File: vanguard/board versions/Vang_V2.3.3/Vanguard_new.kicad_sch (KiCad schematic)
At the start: 94 parts, among them J1 USB_C_Receptacle_USB2.0_16P, J2 Micro_SD_Card_Det1, J3 Conn_02x03_Odd_Even, J4 Conn_01x03, J5 Conn_01x03, J6 Conn_01x03, J7 Conn_01x02_Pin, Q4 BSS138, U1 TPS82130, U10 ATmega4809-A, U12 AP2112K-3.3, U3 ATSAMD11D14A-M, U4 BMP390L, U5 BD1020HFV-TR, U6 AT25DF641A-SH-T, U8 BNO055, U9 TPS61092, Y1 Crystal

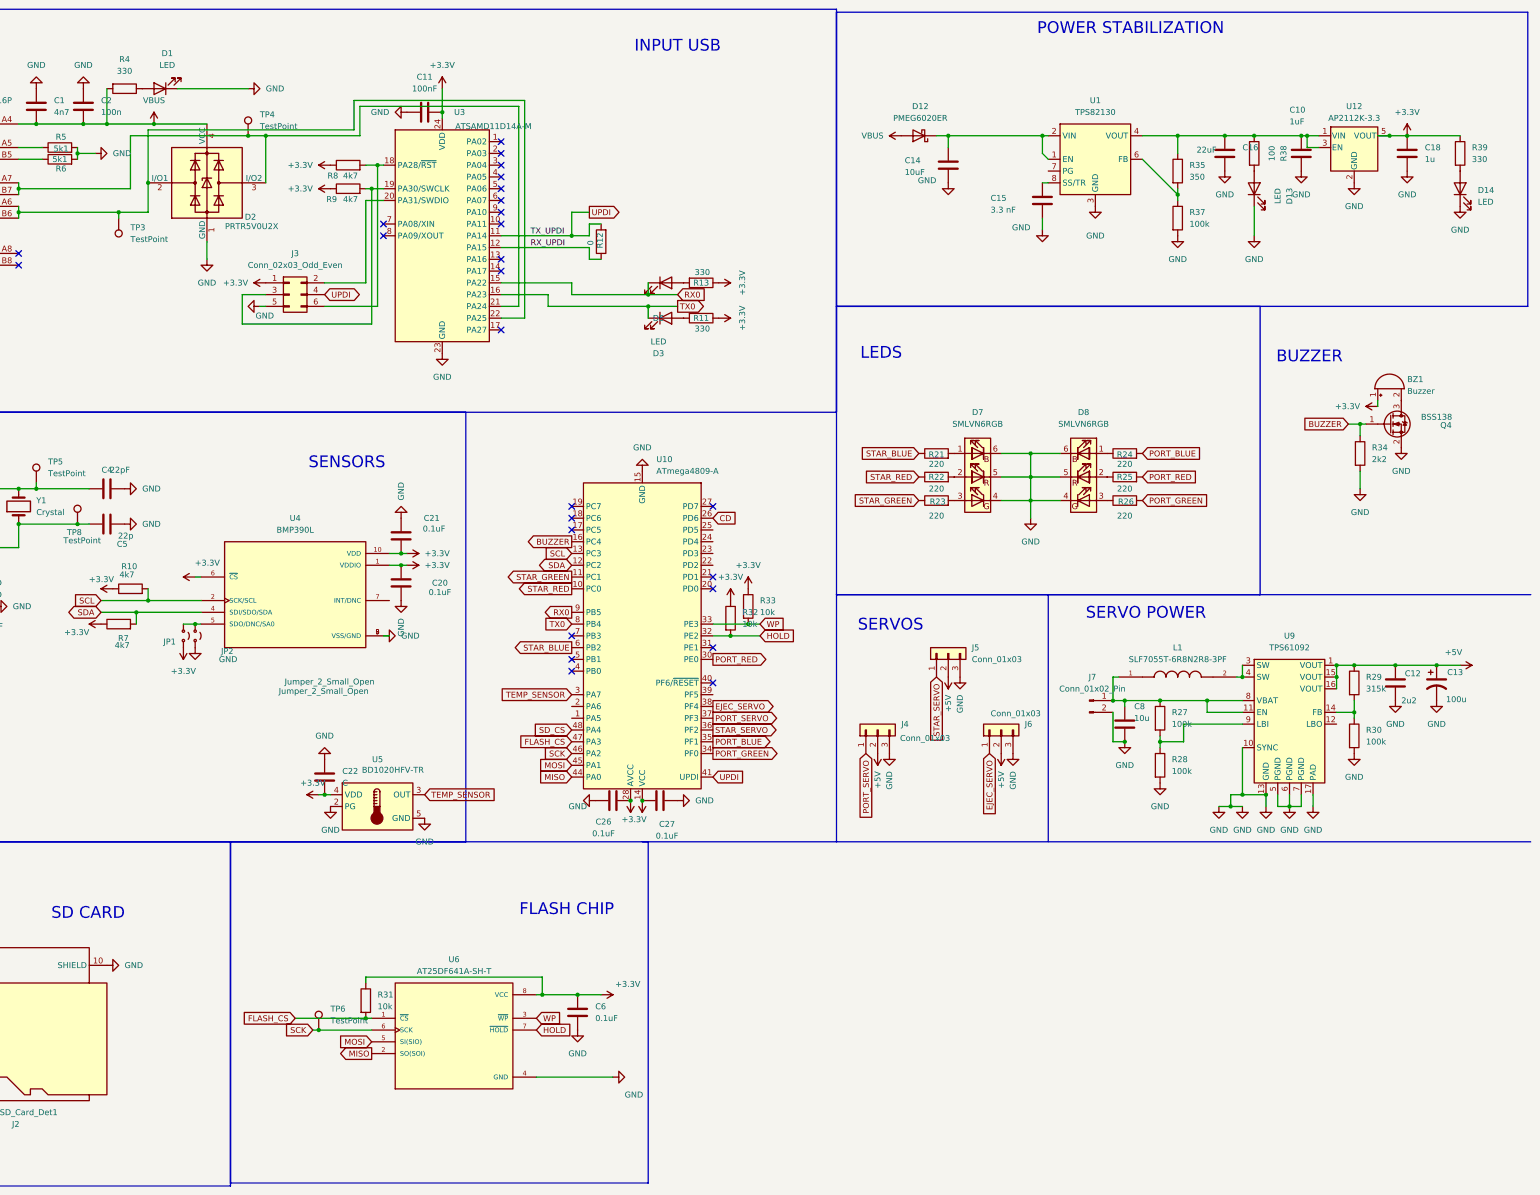
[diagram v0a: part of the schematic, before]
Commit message: added power switch
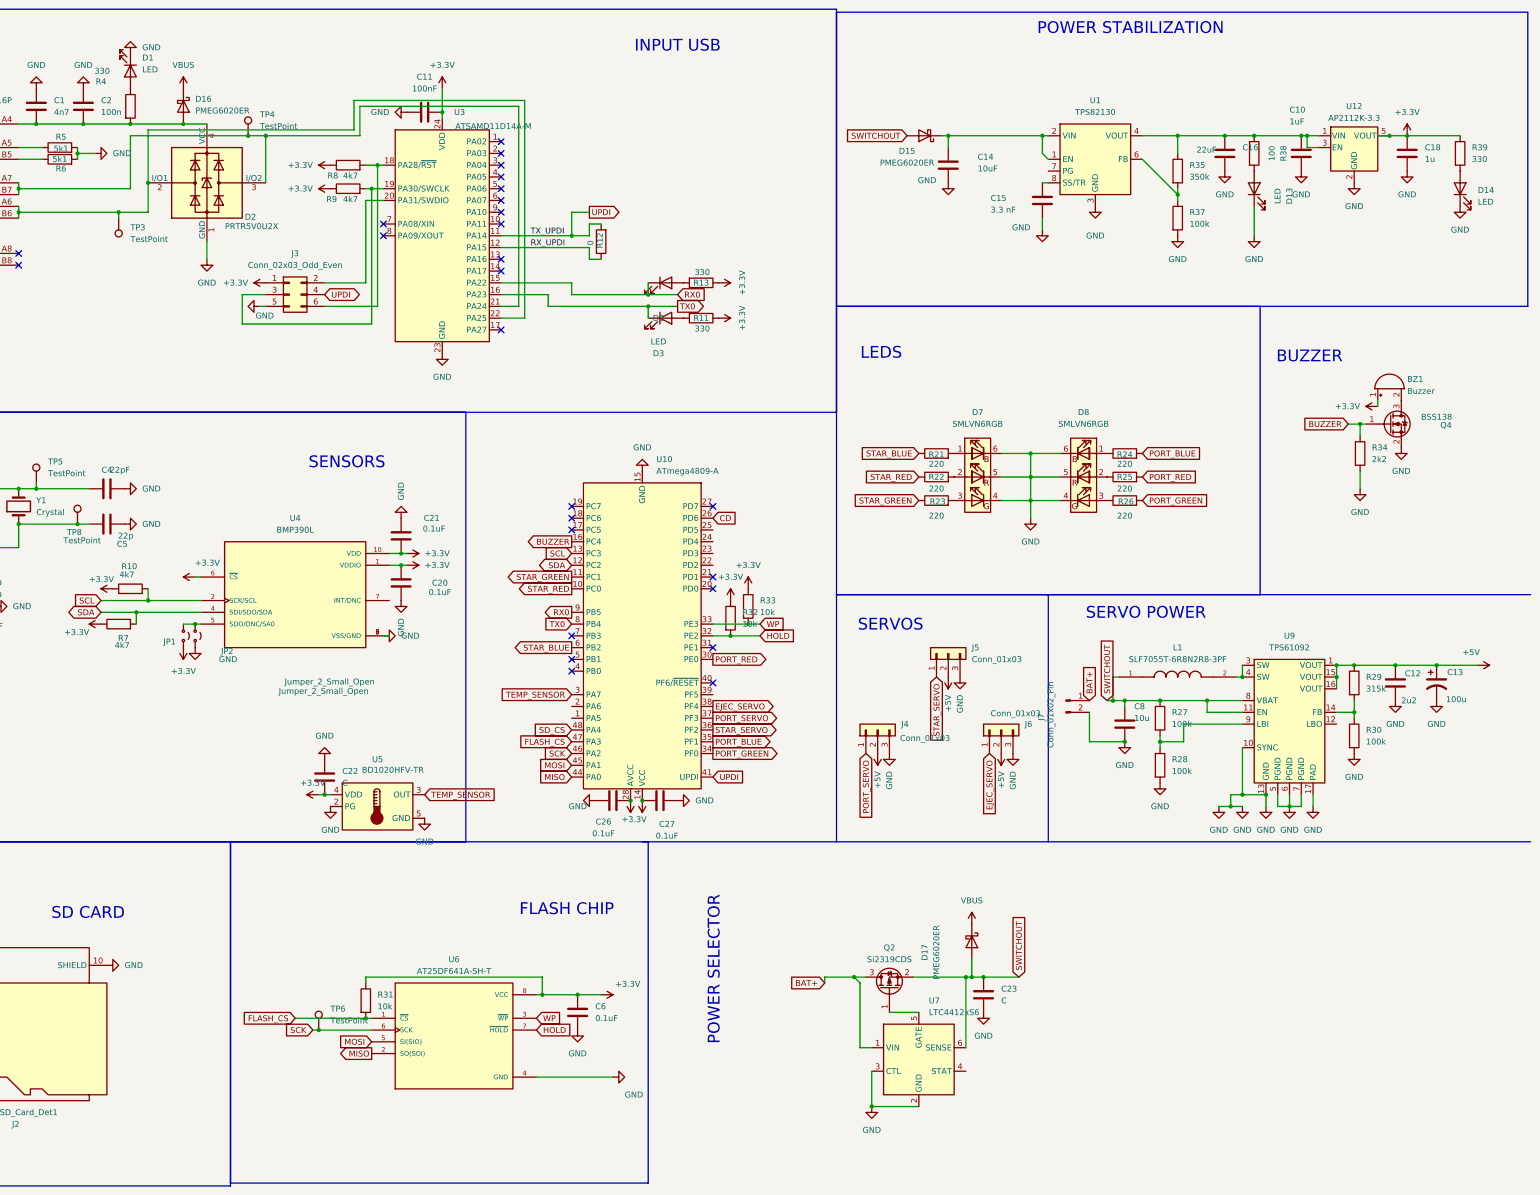
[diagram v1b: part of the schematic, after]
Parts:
- removed D12: PMEG6020ER, Diode_SMD:Nexperia_CFP3_SOD-123W, symbol Diode:PMEG6020ER
- added C23: C, symbol Device:C
- added D15, D16, D17: PMEG6020ER, Diode_SMD:Nexperia_CFP3_SOD-123W, symbol Diode:PMEG6020ER
- added Q2: Si2319CDS, Package_TO_SOT_SMD:SOT-23, symbol Transistor_FET:Si2319CDS
- added U7: LTC4412xS6, Package_TO_SOT_SMD:TSOT-23-6, symbol Power_Management:LTC4412xS6
- R35: value 350 -> 350k
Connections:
- net GND: now also C23.2, U7.2 (GND), U7.3 (CTL)
- net VBUS: now also D16.1 (K), D17.1 (K); no longer C1.2, C2.2, D2.4 (VCC), J1.A4 (VBUS), J1.A9 (VBUS), J1.B4 (VBUS), J1.B9 (VBUS), R4.2
- net SWITCHOUT: now reaches C8.1, L1.1, R27.1, U9.11 (EN), U9.8 (VBAT)
- net SWITCHOUT: now also C23.1, D15.2 (A), D17.2 (A), Q2.2 (S), U7.6 (SENSE); no longer J7.1 (Pin_1)
- net at C14.1, U1.1 (EN), U1.2 (VIN): now also D15.1 (K)
- new net: C1.2, C2.2, D16.2 (A), D2.4 (VCC), J1.A4 (VBUS), J1.A9 (VBUS), J1.B4 (VBUS), J1.B9 (VBUS), R4.2
- new net: Q2.1 (G), U7.5 (GATE)
- new net BAT+: J7.1 (Pin_1), Q2.3 (D), U7.1 (VIN)
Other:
- note added: "POWER SELECTOR"
- moved on the sheet: D1, J7, R4
